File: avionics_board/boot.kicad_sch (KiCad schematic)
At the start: 2 parts, among them SW1 EVP-AA602W

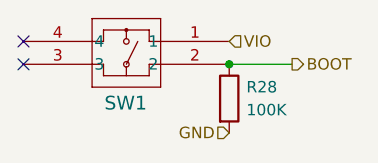
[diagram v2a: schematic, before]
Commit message: QC, add second 3V regulator to AUX, INT pullups on AUX SCI AVI
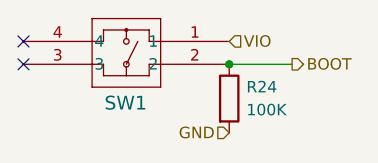
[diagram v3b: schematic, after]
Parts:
- SW1: footprint Project:EVP602AA -> Common:EVP602AA
- renumbered R28 to R24
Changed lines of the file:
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@@
 			)
 		)
-		(property "Footprint" "Project:EVP602AA"
+		(property "Footprint" "Common:EVP602AA"
 			(at 163.83 85.725 0)
 			(effects
@@
 		(dnp no)
 		(fields_autoplaced yes)
-		(property "Reference" "R28"
+		(property "Reference" "R24"
 			(at 165.735 90.8049 0)
 			(effects
@@
 			(project "openlst-hw"
 				(path "/85134265-2435-454a-99c4-e49d8e69c5c2/490a0c5b-9225-4953-ad7a-fe6abb29cde0/a5e0a0bc-1155-4861-b0e5-50e548be6dc2"
-					(reference "R28")
+					(reference "R24")
 					(unit 1)
 				)
@@
 			(project "AVIONICS_BOARD"
 				(path "/f6cc00ab-17f1-4973-862f-7ac95fe70668/00000000-0000-0000-0000-00005ea31c93/ce6e3ce3-97e2-453f-9a1f-2a164dd1fcec"
-					(reference "R41")
-					(unit 1)
-				)
+					(reference "R45")
+					(unit 1)
+				)

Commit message: propate the changes to RF
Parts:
- SW1: symbol Project:EVP-AA602W -> Common:EVP-AA602W
- renumbered R24 to R28
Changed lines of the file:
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@@
 	)
 	(symbol
-		(lib_id "Project:EVP-AA602W")
+		(lib_id "Common:EVP-AA602W")
 		(at 163.83 85.725 0)
 		(mirror y)
@@
 		(instances
 			(project "openlst-hw"
-				(path "/85134265-2435-454a-99c4-e49d8e69c5c2/490a0c5b-9225-4953-ad7a-fe6abb29cde0/a5e0a0bc-1155-4861-b0e5-50e548be6dc2"
-					(reference "SW1")
-					(unit 1)
-				)
-			)
-			(project "openlst-hw"
-				(path "/a863a5ec-a5d4-4f54-be53-e8c01d5e3ac4/53f12969-e593-459a-9671-cc23a5a9aea0/f4ff56ce-2fa2-4b99-a709-c113709260c1/286e6e66-19a5-4c55-b42f-49aa146a8656"
+				(path "/a863a5ec-a5d4-4f54-be53-e8c01d5e3ac4/53f12969-e593-459a-9671-cc23a5a9aea0/f4ff56ce-2fa2-4b99-a709-c113709260c1/05ed6a13-e638-443f-ac45-2ed06780ef6f"
 					(reference "SW1")
 					(unit 1)
@@
 		(dnp no)
 		(fields_autoplaced yes)
-		(property "Reference" "R24"
+		(property "Reference" "R28"
 			(at 165.735 90.8049 0)
 			(effects
@@
 		(instances
 			(project "openlst-hw"
-				(path "/85134265-2435-454a-99c4-e49d8e69c5c2/490a0c5b-9225-4953-ad7a-fe6abb29cde0/a5e0a0bc-1155-4861-b0e5-50e548be6dc2"
-					(reference "R24")
-					(unit 1)
-				)
-			)
-			(project "openlst-hw"
-				(path "/a863a5ec-a5d4-4f54-be53-e8c01d5e3ac4/53f12969-e593-459a-9671-cc23a5a9aea0/f4ff56ce-2fa2-4b99-a709-c113709260c1/286e6e66-19a5-4c55-b42f-49aa146a8656"
-					(reference "R38")
-					(unit 1)
-				)
+				(path "/a863a5ec-a5d4-4f54-be53-e8c01d5e3ac4/53f12969-e593-459a-9671-cc23a5a9aea0/f4ff56ce-2fa2-4b99-a709-c113709260c1/05ed6a13-e638-443f-ac45-2ed06780ef6f"
+					(reference "R28")
+					(unit 1)
+				)

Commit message: tweaks before merge
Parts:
- renumbered R28 to R24
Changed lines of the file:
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@@
+			)
+		)
+		(property "MANUFACTURER" ""
+			(at 163.83 85.725 0)
+			(effects
+				(font
+					(size 1.27 1.27)
+				)
+				(hide yes)
+			)
+		)
+		(property "MAXIMUM_PACKAGE_HEIGHT" ""
+			(at 163.83 85.725 0)
+			(effects
+				(font
+					(size 1.27 1.27)
+				)
+				(hide yes)
+			)
+		)
+		(property "PARTREV" ""
+			(at 163.83 85.725 0)
+			(effects
+				(font
+					(size 1.27 1.27)
+				)
+				(hide yes)
+			)
+		)
+		(property "STANDARD" ""
+			(at 163.83 85.725 0)
+			(effects
+				(font
+					(size 1.27 1.27)
+				)
+				(hide yes)
 			)
 		)
@@
 		)
 		(instances
+			(project "aux_board"
+				(path "/85134265-2435-454a-99c4-e49d8e69c5c2/490a0c5b-9225-4953-ad7a-fe6abb29cde0/a5e0a0bc-1155-4861-b0e5-50e548be6dc2"
+					(reference "SW1")
+					(unit 1)
+				)
+			)
 			(project "openlst-hw"
 				(path "/a863a5ec-a5d4-4f54-be53-e8c01d5e3ac4/53f12969-e593-459a-9671-cc23a5a9aea0/f4ff56ce-2fa2-4b99-a709-c113709260c1/05ed6a13-e638-443f-ac45-2ed06780ef6f"
@@
 		(dnp no)
 		(fields_autoplaced yes)
-		(property "Reference" "R28"
+		(property "Reference" "R24"
 			(at 165.735 90.8049 0)
 			(effects
@@
 			)
 		)
+		(property "MANUFACTURER" ""
+			(at 163.83 92.075 0)
+			(effects
+				(font
+					(size 1.27 1.27)
+				)
+				(hide yes)
+			)
+		)
+		(property "MAXIMUM_PACKAGE_HEIGHT" ""
+			(at 163.83 92.075 0)
+			(effects
+				(font
+					(size 1.27 1.27)
+				)
+				(hide yes)
+			)
+		)
+		(property "PARTREV" ""
+			(at 163.83 92.075 0)
+			(effects
+				(font
+					(size 1.27 1.27)
+				)
+				(hide yes)
+			)
+		)
+		(property "STANDARD" ""
+			(at 163.83 92.075 0)
+			(effects
+				(font
+					(size 1.27 1.27)
+				)
+				(hide yes)
+			)
+		)
 		(pin "2"
 		)
@@
 		)
 		(instances
+			(project "aux_board"
+				(path "/85134265-2435-454a-99c4-e49d8e69c5c2/490a0c5b-9225-4953-ad7a-fe6abb29cde0/a5e0a0bc-1155-4861-b0e5-50e548be6dc2"
+					(reference "R24")
+					(unit 1)
+				)
+			)
 			(project "openlst-hw"
 				(path "/a863a5ec-a5d4-4f54-be53-e8c01d5e3ac4/53f12969-e593-459a-9671-cc23a5a9aea0/f4ff56ce-2fa2-4b99-a709-c113709260c1/05ed6a13-e638-443f-ac45-2ed06780ef6f"

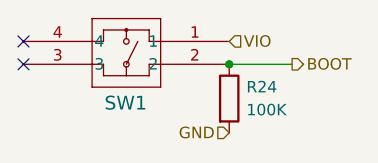
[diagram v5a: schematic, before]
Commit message: local switches and monitors for SCI and RF
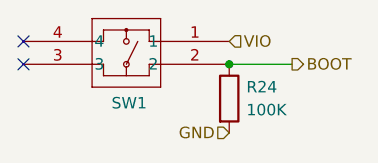
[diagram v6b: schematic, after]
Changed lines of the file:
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@@
 			(effects
 				(font
-					(size 1.524 1.524)
+					(size 1.27 1.27)
 				)
 				(justify left)
@@
 			(effects
 				(font
-					(size 1.524 1.524)
+					(size 1.27 1.27)
 				)
 				(justify left)
@@
 			(project "openlst-hw"
 				(path "/a863a5ec-a5d4-4f54-be53-e8c01d5e3ac4/53f12969-e593-459a-9671-cc23a5a9aea0/f4ff56ce-2fa2-4b99-a709-c113709260c1/05ed6a13-e638-443f-ac45-2ed06780ef6f"
-					(reference "R28")
+					(reference "R42")
 					(unit 1)
 				)
@@
 			(project "sci_board"
 				(path "/b4b2c88d-f6cd-4e60-862d-e21f68728580/840799ac-4fe6-4a8e-96a2-299affeec8e4/9ad2e03f-9236-48b3-ba37-0d7f891d93a5"
-					(reference "R41")
-					(unit 1)
-				)
+					(reference "R46")
+					(unit 1)
+				)
